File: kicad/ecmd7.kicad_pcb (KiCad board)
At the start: 4 copper layers, 120 x 90 mm, 250 parts, among them J1 PMOD_SPI_ENC, J2 PMOD_ADC_MPIO, J3 PMOD_DRV, J4 Conn_01x02_Socket, J5 Encoder, J6 12V, J7 RS422/BISS-C, J8 5V, Q1 IRFS3806, Q10 BSC098N10NS5, Q11 MMBT3904, Q12 MMBT3904, Q2 IRFS3806, Q3 IRFS3806, Q4 IRFS3806, Q5 IRFS3806, Q6 IRFS3806, Q7 BSC098N10NS5, Q8 BSC098N10NS5, Q9 BSC098N10NS5, U1 TMC6200-TA, U10 FIN1002M5X, U11 FIN1002M5X, U12 FIN1002M5X, U13 ADM3490ExR, U14 LM5118MH, U15 74LVC1G139, U16 MB85RS1MT, U17 TMP122AIDBVR, U2 MCP33151-05T-E/MN, U3 LM5118MH, U4 MCP33151-05T-E/MN, U5 MCP33151-05T-E/MN, U6 TLV71318PDBV, U7 MCP33151-05T-E/MN, U9 LT1616ES6#TRPBF

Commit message: Cleanup schematic
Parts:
- R1, R2, R3, R4, R7: value 0.47 -> 100m
- R12, R44: value 62k -> 68k
- R31, R75: value 470 -> 4.7k
- R48: value 470 -> 330
- R49, R53, R76, R9: value 330 -> 4.7k
- R50: value 470 -> 820
- R8: value 10 -> 100m
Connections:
- net /ADC+IO/A_LS_N renamed /Sensors/A_LS_N
- net /ADC+IO/A_LS_P renamed /Sensors/A_LS_P
- net /ADC+IO/B_LS_N renamed /Sensors/B_LS_N
- net /ADC+IO/B_LS_P renamed /Sensors/B_LS_P
- net /ADC+IO/Z_LS_N renamed /Sensors/Z_LS_N
- net /ADC+IO/Z_LS_P renamed /Sensors/Z_LS_P
- net /ADC+IO/~{CS_FRAM} renamed /~{CS_FRAM}
- net /ADC+IO/~{CS_TMP} renamed /~{CS_TMP}
- net AD_SCK renamed /AD_SCK
- net AD_SDO_IU renamed /AD_SDO_IU
- net AD_SDO_IV renamed /AD_SDO_IV
- net AD_SDO_IW renamed /AD_SDO_IW
- net AD_SDO_VBUS renamed /AD_SDO_VBUS
- net CS0 renamed /CS0
- net CS1 renamed /CS1
- net ENC_A renamed /ENC_A
- net ENC_A_N renamed /ENC_A_N
- net ENC_A_P renamed /ENC_A_P
- net ENC_B renamed /ENC_B
- net ENC_B_N renamed /ENC_B_N
- net ENC_B_P renamed /ENC_B_P
- net ENC_Z renamed /ENC_Z
- net ENC_Z_N renamed /ENC_Z_N
- net ENC_Z_P renamed /ENC_Z_P
- net I_U renamed /ADC/I_U
- net I_V renamed /ADC/I_V
- net I_W renamed /ADC/I_W
- net Net-(JU1-Pin_1) renamed /Power Stage/U
- net Net-(JV1-Pin_1) renamed /Power Stage/V
- net Net-(JW1-Pin_1) renamed /Power Stage/W
- net RS422_RX renamed /RS422_RX
- net RS422_RX_A renamed /RS422_RX_A
- net RS422_RX_B renamed /RS422_RX_B
- net RS422_TX renamed /RS422_TX
- net RS422_TX_A renamed /RS422_TX_A
- net RS422_TX_B renamed /RS422_TX_B
- net SPI_SCK renamed /SPI_SCK
- net SPI_SDI renamed /SPI_SDI
- net SPI_SDO renamed /SPI_SDO
- net ~{CS_AD} renamed /~{CS_AD}
- net ~{CS_DRV} renamed /~{CS_DRV}

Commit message: Cleanup schematic, add busses
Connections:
- net /AD_SCK renamed /ADC/ADC.SCLK
- net /AD_SDO_IU renamed /ADC/ADC.MOSI0
- net /AD_SDO_IV renamed /ADC/ADC.MOSI1
- net /AD_SDO_IW renamed /ADC/ADC.MOSI2
- net /AD_SDO_VBUS renamed /ADC/ADC.MOSI3
- net /CS0 renamed /Memory + CS Decoder/CS0
- net /CS1 renamed /Memory + CS Decoder/CS1
- net /DRV_EN renamed /Power Stage/EN
- net /FAULT renamed /Power Stage/FAULT
- net /SPI_SCK renamed /Memory + CS Decoder/SCLK
- net /SPI_SDI renamed /Memory + CS Decoder/MOSI
- net /SPI_SDO renamed /Memory + CS Decoder/MISO
- net /UH renamed /Power Stage/UH
- net /UL renamed /Power Stage/UL
- net /VH renamed /Power Stage/VH
- net /VL renamed /Power Stage/VL
- net /WH renamed /Power Stage/WH
- net /WL renamed /Power Stage/WL
- net /~{CS_AD} renamed /ADC/ADC.~{CS}
- net /~{CS_DRV} renamed /Memory + CS Decoder/~{CS1}
- net /~{CS_FRAM} renamed /Memory + CS Decoder/~{CS2}
- net /~{CS_TMP} renamed /Memory + CS Decoder/~{CS3}

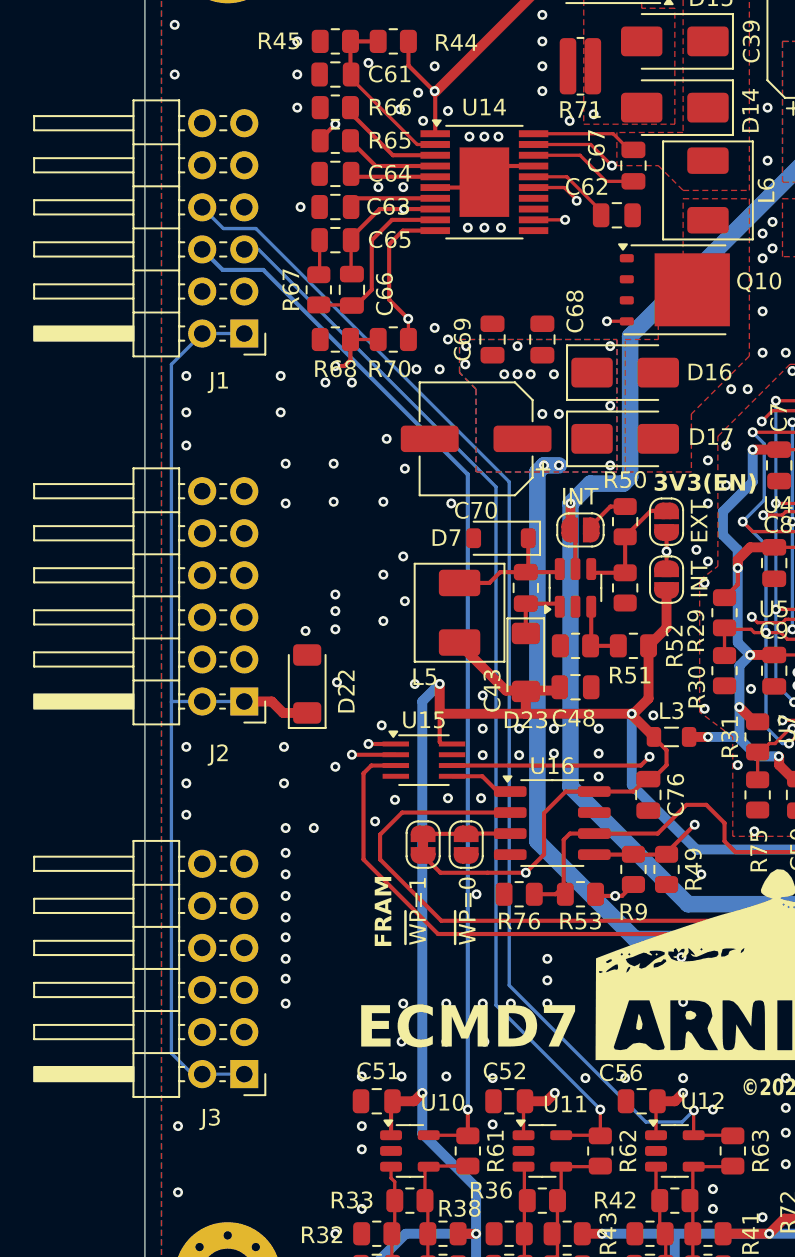
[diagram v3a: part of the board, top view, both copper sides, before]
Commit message: General schematic cleanup
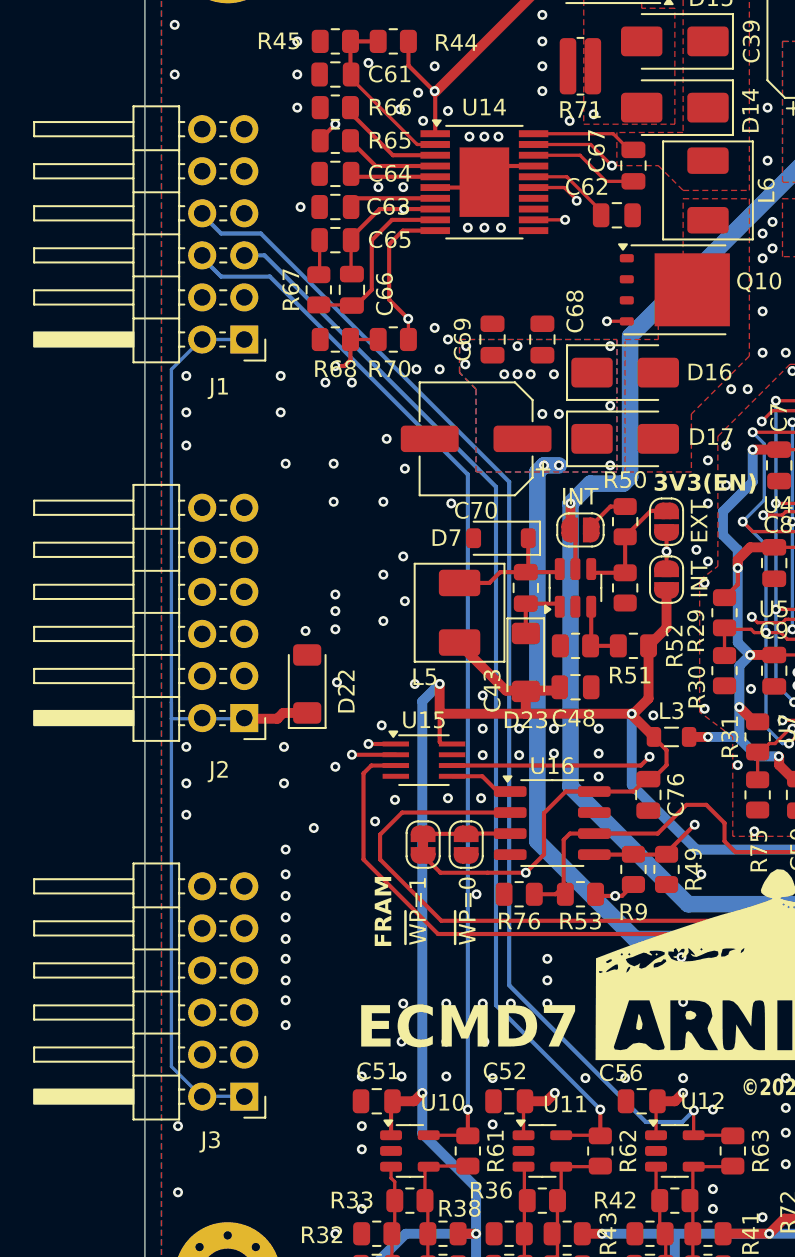
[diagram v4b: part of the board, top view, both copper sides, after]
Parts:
- R6: value 0.47 -> 100m
- R8: value 100m -> 10
- moved J3 1.36 mm to (66.0, 114.2)
- moved J2 1.00 mm to (66.0, 91.4)
- moved J1 0.36 mm to (66.0, 68.5)
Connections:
- net /ADC/ADC.MOSI0 renamed /ADC.MOSI0
- net /ADC/ADC.MOSI1 renamed /ADC.MOSI1
- net /ADC/ADC.MOSI2 renamed /ADC.MOSI2
- net /ADC/ADC.MOSI3 renamed /ADC.MOSI3
- net /ADC/ADC.SCLK renamed /ADC.SCLK
- net /ADC/ADC.~{CS} renamed /ADC.~{CS}
- net /Memory + CS Decoder/CS0 renamed /CS0
- net /Memory + CS Decoder/CS1 renamed /CS1
- net /Memory + CS Decoder/MISO renamed /MISO
- net /Memory + CS Decoder/MOSI renamed /MOSI
- net /Memory + CS Decoder/SCLK renamed /SCLK
- net /Memory + CS Decoder/~{CS1} renamed /~{CS1}
- net /Memory + CS Decoder/~{CS2} renamed /~{CS2}
- net /Memory + CS Decoder/~{CS3} renamed /~{CS3}
- net /Power Stage/EN renamed /EN
- net /Power Stage/FAULT renamed /FAULT
- net /Power Stage/UH renamed /UH
- net /Power Stage/UL renamed /UL
- net /Power Stage/VH renamed /VH
- net /Power Stage/VL renamed /VL
- net /Power Stage/WH renamed /WH
- net /Power Stage/WL renamed /WL
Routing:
- net (no net): track 0.00 -> 124.4 mm, vias 0 -> 2
- net /VH: track 64.2 -> 0.00 mm, vias 1 -> 0
- net /WH: track 63.8 -> 0.00 mm, vias 1 -> 0
- net +3.3V_IO: track 91.0 -> 93.6 mm
- net /RS422_RX: track 73.6 -> 71.2 mm
- net /UH: track 66.7 -> 64.9 mm
- net /RS422_TX: track 75.6 -> 74.2 mm
- net /EN: track 77.9 -> 76.6 mm
- net /FAULT: track 86.9 -> 87.5 mm
- net GND: vias 281 -> 280
